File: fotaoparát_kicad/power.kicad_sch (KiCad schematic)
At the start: 41 parts

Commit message: Pridani krystalu
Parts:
- renumbered BAT+1 to BAT_IN1, BAT-1 to BAT_OUT1
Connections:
- net VDD_MIPI_DPHY is gone; now on net VDDO_3: C34.1, C39.1
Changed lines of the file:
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@@
+	(wire
+		(pts
+			(xy 36.83 163.83) (xy 35.56 163.83)
+		)
+		(stroke
+			(width 0)
+			(type default)
+		)
+	)
 	(wire
 		(pts
@@
 	(wire
 		(pts
+			(xy 22.86 163.83) (xy 22.86 165.1)
+		)
+		(stroke
+			(width 0)
+			(type default)
+		)
+	)
+	(wire
+		(pts
 			(xy 213.36 55.88) (xy 241.3 55.88)
 		)
@@
 	(wire
 		(pts
+			(xy 35.56 163.83) (xy 35.56 165.1)
+		)
+		(stroke
+			(width 0)
+			(type default)
+		)
+	)
+	(wire
+		(pts
 			(xy 241.3 44.45) (xy 241.3 45.72)
 		)
@@
 		(pts
 			(xy 78.74 55.88) (xy 78.74 62.23)
+		)
+		(stroke
+			(width 0)
+			(type default)
+		)
+	)
+	(wire
+		(pts
+			(xy 50.8 165.1) (xy 48.26 165.1)
 		)
 		(stroke
@@
 	(hierarchical_label "VDDO_FLASH"
 		(shape input)
-		(at 22.86 165.1 0)
+		(at 22.86 163.83 0)
 		(effects
 			(font
@@
 	(hierarchical_label "VDDO_PSRAM"
 		(shape input)
-		(at 35.56 165.1 0)
-		(effects
-			(font
-				(size 1.27 1.27)
-			)
-			(justify left)
-		)
-	)
-	(hierarchical_label "VDD_MIPI_DPHY"
-		(shape input)
-		(at 146.05 144.78 0)
+		(at 36.83 163.83 0)
 		(effects
 			(font
@@
 	(hierarchical_label "VDDO_3"
 		(shape input)
-		(at 48.26 165.1 0)
+		(at 50.8 165.1 0)
 		(effects
 			(font
@@
 		(shape input)
 		(at 48.26 124.46 0)
+		(effects
+			(font
+				(size 1.27 1.27)
+			)
+			(justify left)
+		)
+	)
+	(hierarchical_label "VDDO_3"
+		(shape input)
+		(at 146.05 144.78 0)
 		(effects
 			(font
@@
 		(on_board yes)
 		(dnp no)
-		(property "Reference" "BAT-1"
+		(property "Reference" "BAT_OUT1"
 			(at 89.154 64.77 0)
 			(effects
@@
 			(project "fotaoparát"
 				(path "/0ab33720-0b6a-449c-80c0-2b7abe4d9450/04ebdae2-67d7-4749-bd3e-f9c05089f6fb"
-					(reference "BAT-1")
+					(reference "BAT_OUT1")
 					(unit 1)
 				)
@@
 		(on_board yes)
 		(dnp no)
-		(property "Reference" "BAT+1"
+		(property "Reference" "BAT_IN1"
 			(at 28.194 22.86 0)
 			(effects
@@
 			(project "fotaoparát"
 				(path "/0ab33720-0b6a-449c-80c0-2b7abe4d9450/04ebdae2-67d7-4749-bd3e-f9c05089f6fb"
-					(reference "BAT+1")
+					(reference "BAT_IN1")
 					(unit 1)
 				)

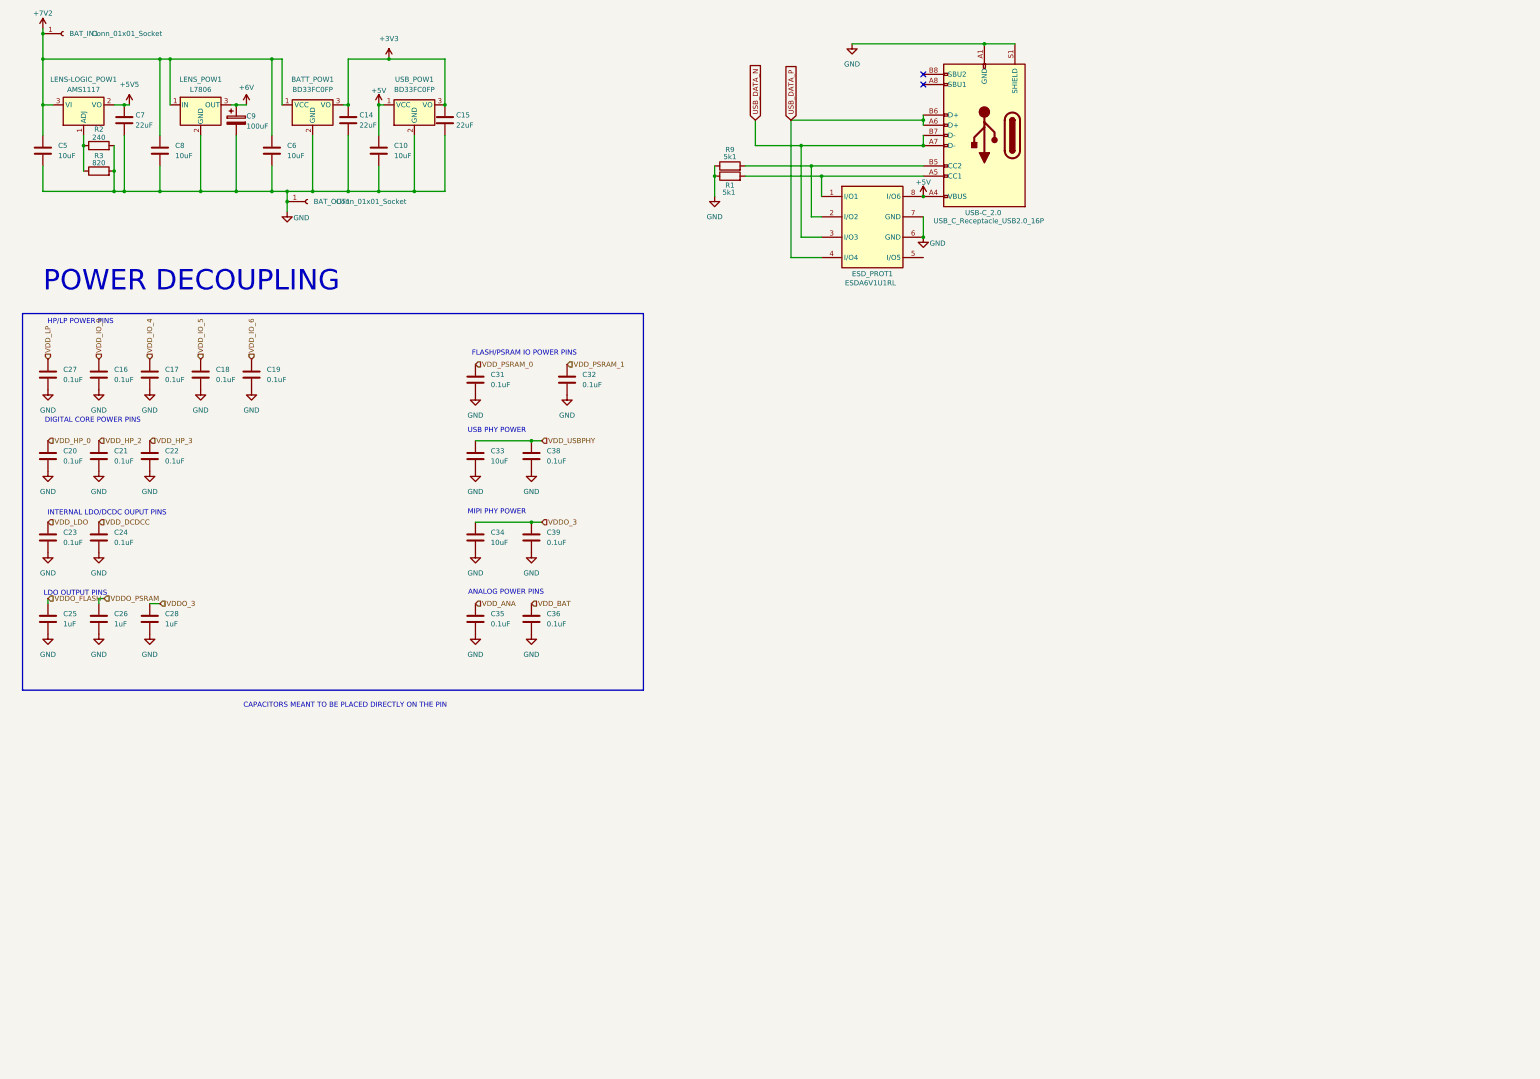
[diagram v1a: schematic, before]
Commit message: Předělání powerrials,  přidání malého pcb na spousť foťáku
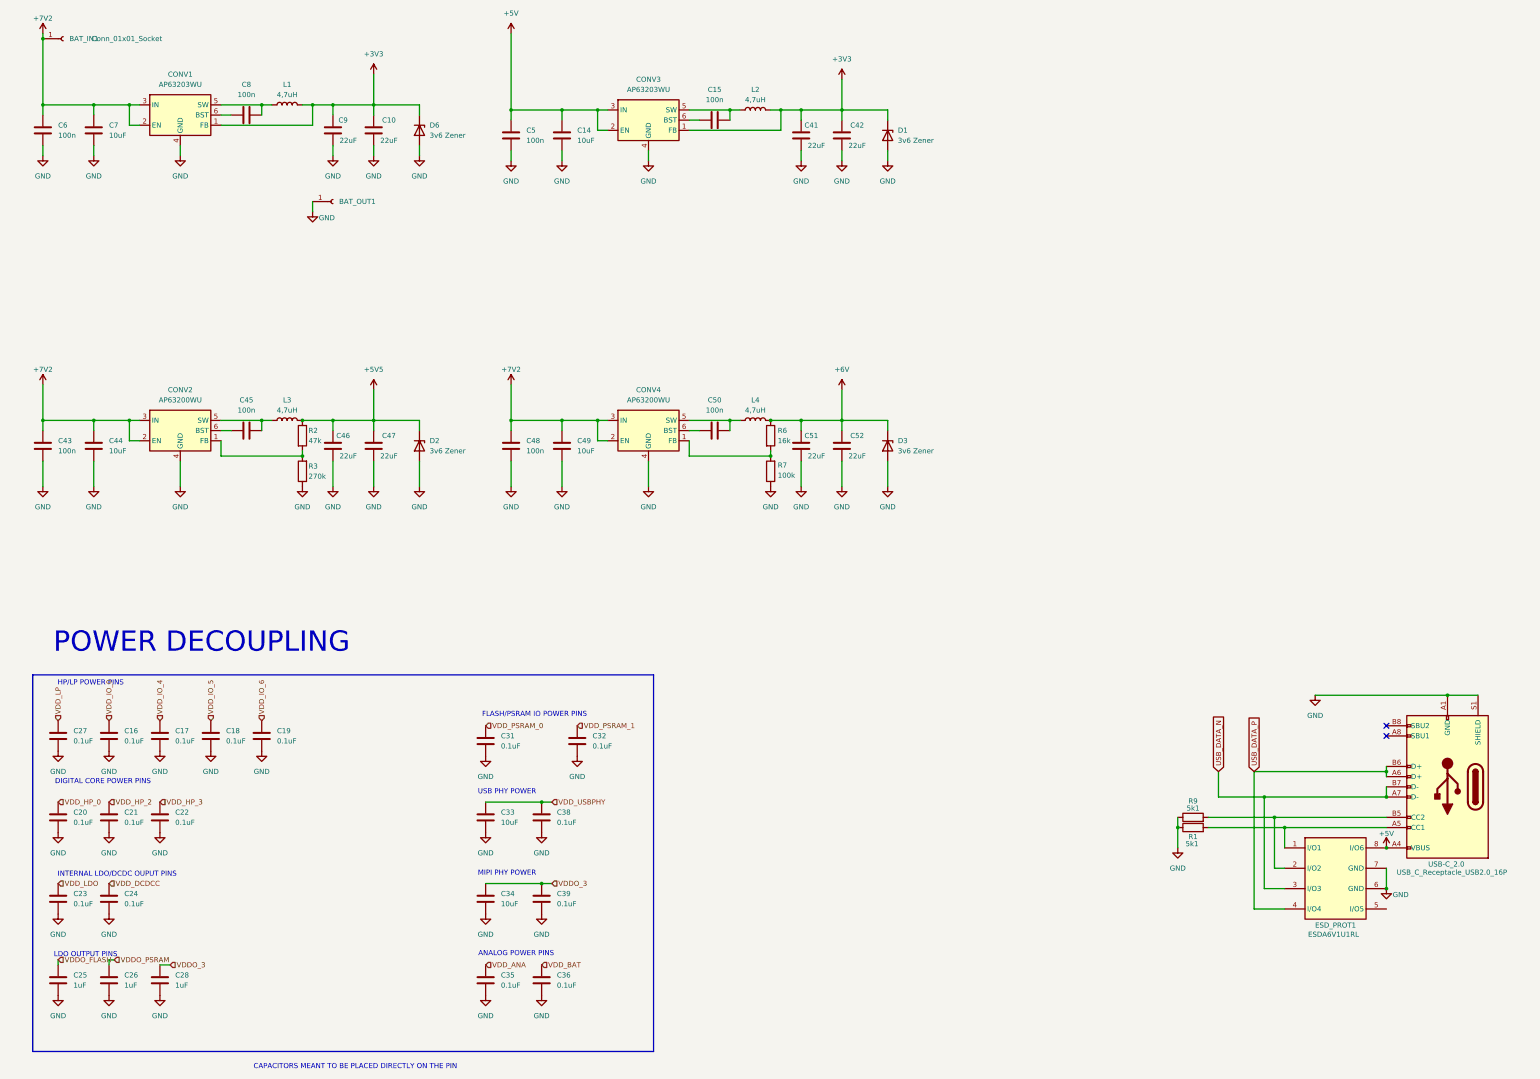
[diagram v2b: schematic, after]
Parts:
- removed BATT_POW1, USB_POW1: BD33FC0FP, Package_TO_SOT_SMD:TO-252-2, symbol Regulator_Linear:BD33FC0FP
- removed C9: 100uF, Capacitor_SMD:CP_Elec_6.3x5.4, symbol Device:C_Polarized
- removed LENS-LOGIC_POW1: AMS1117, Package_TO_SOT_SMD:SOT-223-3_TabPin2, symbol Regulator_Linear:AMS1117
- removed LENS_POW1: L7806, Package_TO_SOT_THT:TO-220-3_Horizontal_TabDown, symbol Regulator_Linear:L7806
- added C41, C42, C46, C47, C51, C52, C9: 22uF, Capacitor_SMD:C_0603_1608Metric, symbol Device:C
- added C43, C45, C48, C50: 100n, Capacitor_SMD:C_0603_1608Metric, symbol Device:C
- added C44, C49: 10uF, Capacitor_SMD:C_0603_1608Metric, symbol Device:C
- added CONV1, CONV3: AP63203WU, Package_TO_SOT_SMD:TSOT-23-6, symbol Regulator_Switching:AP63203WU
- added CONV2, CONV4: AP63200WU, Package_TO_SOT_SMD:TSOT-23-6, symbol Regulator_Switching:AP63200WU
- added D1, D2, D3, D6: 3v6 Zener, Diode_SMD:D_SOD-123, symbol Device:D_Zener
- added L1, L2, L3, L4: 4,7uH, Inductor_SMD:L_0603_1608Metric, symbol Device:L
- added R6: 16k, Resistor_SMD:R_0603_1608Metric, symbol Device:R
- added R7: 100k, Resistor_SMD:R_0603_1608Metric, symbol Device:R
- C10: value 10uF -> 22uF; footprint Capacitor_SMD:C_0201_0603Metric -> Capacitor_SMD:C_0603_1608Metric; LCSC (none) -> C59461; LCSC Part (none) -> C59461; Type (none) -> Basic
- C14, C7: value 22uF -> 10uF; footprint Capacitor_SMD:C_0201_0603Metric -> Capacitor_SMD:C_0603_1608Metric; LCSC (none) -> C19702; LCSC Part (none) -> C19702; Type (none) -> Basic
- C15: value 22uF -> 100n; footprint Capacitor_SMD:C_0201_0603Metric -> Capacitor_SMD:C_0603_1608Metric; LCSC (none) -> C14663; LCSC Part (none) -> C14663; Type (none) -> Basic
- C5, C6, C8: value 10uF -> 100n; footprint Capacitor_SMD:C_0201_0603Metric -> Capacitor_SMD:C_0603_1608Metric; LCSC (none) -> C14663; LCSC Part (none) -> C14663; Type (none) -> Basic
- R2: value 240 -> 47k
- R3: value 820 -> 270k
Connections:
- net +3V3: now also C10.2, C41.2, C42.2, C9.2, CONV1.1 (FB), CONV3.1 (FB), D1.1 (K), D6.1 (K), L1.2, L2.2; no longer C14.1, C15.1
- net +5V: now also C14.2, C5.2, CONV3.2 (EN), CONV3.3 (IN); no longer C10.1
- net +5V5: now also R2.1, C46.2, C47.2, D2.1 (K), L3.2; no longer C7.1
- net +6V: now also C51.2, C52.2, D3.1 (K), L4.2, R6.1
- net +7V2: now also C6.2, C7.2, C43.2, C44.2, C48.2, C49.2, CONV1.2 (EN), CONV1.3 (IN), CONV2.2 (EN), CONV2.3 (IN), CONV4.2 (EN), CONV4.3 (IN); no longer C5.1, C6.1, C8.1
- net GND: now also C10.1, C14.1, C5.1, C6.1, C7.1, R3.1, C41.1, C42.1, C43.1, C44.1, C46.1, C47.1, C48.1, C49.1, C51.1, C52.1, C9.1, CONV1.4 (GND), CONV2.4 (GND), CONV3.4 (GND), CONV4.4 (GND), D1.2 (A), D2.2 (A), D3.2 (A), D6.2 (A), R7.1; no longer C10.2, C14.2, C15.2, C5.2, C6.2, C7.2, C8.2, R2.2, R3.2
- new net: C8.1, CONV1.6 (BST)
- new net: C8.2, CONV1.5 (SW), L1.1
- new net: CONV2.1 (FB), R2.2, R3.2
- new net: C50.2, CONV4.5 (SW), L4.1
- new net: C45.1, CONV2.6 (BST)
- new net: C45.2, CONV2.5 (SW), L3.1
- new net: CONV4.1 (FB), R6.2, R7.2
- new net: C50.1, CONV4.6 (BST)
- new net: C15.1, CONV3.6 (BST)
- new net: C15.2, CONV3.5 (SW), L2.1
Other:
- moved on the sheet: BAT_IN1, BAT_OUT1, C16, C17, C18, C19, C20, C21, C22, C23, C24, C25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

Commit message: XDD NEVIM ZABIJU SE
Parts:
- removed C14: 10uF, Capacitor_SMD:C_0603_1608Metric, symbol Device:C
- removed C15, C5: 100n, Capacitor_SMD:C_0603_1608Metric, symbol Device:C
- removed C41, C42: 22uF, Capacitor_SMD:C_0603_1608Metric, symbol Device:C
- removed CONV3: AP63203WU, Package_TO_SOT_SMD:TSOT-23-6, symbol Regulator_Switching:AP63203WU
- removed D1: 3v6 Zener, Diode_SMD:D_SOD-123, symbol Device:D_Zener
- removed L2: 4,7uH, Inductor_SMD:L_0603_1608Metric, symbol Device:L
- added D1, D4: D_Schottky, Diode_SMD:D_0805_2012Metric, symbol Device:D_Schottky
- added J2: Conn_01x12_Pin, Connector_FFC-FPC:Hirose_FH12-11S-0.5SH_1x11-1MP_P0.50mm_Horizontal, symbol Connector:Conn_01x12_Pin
- added J3: Conn_01x12_Pin, symbol Connector:Conn_01x12_Pin
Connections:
- net +5V: now also D4.2 (A)
- net +7V2: now also D1.2 (A); no longer C6.2, C7.2, CONV1.2 (EN), CONV1.3 (IN)
- new net: C6.2, C7.2, CONV1.2 (EN), CONV1.3 (IN), D1.1 (K), D4.1 (K)
- new net: J2.1 (Pin_1), J3.1 (Pin_1)
- new net: J2.10 (Pin_10), J3.10 (Pin_10)
- new net: J2.11 (Pin_11), J3.11 (Pin_11)
- new net: J2.12 (Pin_12), J3.12 (Pin_12)
- new net: J2.2 (Pin_2), J3.2 (Pin_2)
- new net: J2.3 (Pin_3), J3.3 (Pin_3)
- new net: J2.4 (Pin_4), J3.4 (Pin_4)
- new net: J2.5 (Pin_5), J3.5 (Pin_5)
- new net: J2.6 (Pin_6), J3.6 (Pin_6)
- new net: J2.7 (Pin_7), J3.7 (Pin_7)
- new net: J2.8 (Pin_8), J3.8 (Pin_8)
- new net: J2.9 (Pin_9), J3.9 (Pin_9)
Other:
- moved on the sheet: BAT_IN1

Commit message: Pridani asi poloviny lscs cisel
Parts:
- removed J2: Conn_01x12_Pin, Connector_FFC-FPC:Hirose_FH12-11S-0.5SH_1x11-1MP_P0.50mm_Horizontal, symbol Connector:Conn_01x12_Pin
- removed J3: Conn_01x12_Pin, symbol Connector:Conn_01x12_Pin
- BAT_IN1, BAT_OUT1: now left out of the parts list
- C10, C46, C47, C51, C52, C9: LSCS Number (none) -> C2762594
- C16, C17, C18, C19, C20, C21, C22, C23, C24, C27, C31, C32, C35, C36, C38, C39: value 0.1uF -> 100nF; LSCS Number (none) -> C668346
- C25, C26, C28: LSCS Number (none) -> C307385
- C33, C34, C44, C49, C7: LSCS Number (none) -> C962136
- C43, C45, C48, C50, C6, C8: value 100n -> 100nF; LSCS Number (none) -> C66501
- CONV1: LSCS Number (none) -> C780769
- CONV2, CONV4: LSCS Number (none) -> C2071868
- D1, D4: LSCS Number (none) -> C143773
- D2, D3, D6: LSCS Number (none) -> C173412
- ESD_PROT1: LSCS Number (none) -> C118278

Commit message: PRidani (skoro) vsech lscs cisel, krystal je spatne ale pcb mam doma udelane jeste jinak, takze pridam a preroutuju pozdeji.
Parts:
- D2: value 3v6 Zener -> 5V7 Zener; LSCS Number C173412 -> C2993567
- D3: value 3v6 Zener -> 6V2 Zener; LSCS Number C173412 -> C397931
- L1: value 4,7uH -> 3,9uH; LSCS Number (none) -> C251964
- L3, L4: value 4,7uH -> 10uH; LSCS Number (none) -> C713281
- R1, R9: LSCS Number (none) -> C105580
- R2: LSCS Number (none) -> C105579
- R3: LSCS Number (none) -> C22965
- R6: LSCS Number (none) -> C137788
- R7: LSCS Number (none) -> C14675
- USB-C_2.0: LSCS Number (none) -> C53055681
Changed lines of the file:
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@@
 			)
 		)
+		(property "LSCS Number" "C22965"
+			(at 86.36 132.08 0)
+			(effects
+				(font
+					(size 1.27 1.27)
+				)
+				(hide yes)
+			)
+		)
 		(pin "2"
 		)
@@
 			)
 		)
-		(property "Value" "3v6 Zener"
+		(property "Value" "5V7 Zener"
 			(at 118.11 126.9999 90)
 			(effects
@@
 			)
 		)
-		(property "LSCS Number" "C173412"
+		(property "LSCS Number" "C2993567"
 			(at 115.57 125.73 90)
 			(effects
@@
 			)
 		)
-		(property "Value" "4,7uH"
+		(property "Value" "10uH"
 			(at 199.39 116.84 90)
 			(effects
@@
 			)
 		)
+		(property "LSCS Number" "C713281"
+			(at 199.39 119.38 90)
+			(effects
+				(font
+					(size 1.27 1.27)
+				)
+				(hide yes)
+			)
+		)
 		(pin "1"
 		)
@@
 			)
 		)
-		(property "Value" "3v6 Zener"
+		(property "Value" "6V2 Zener"
 			(at 234.95 126.9999 90)
 			(effects
@@
 			)
 		)
-		(property "LSCS Number" "C173412"
+		(property "LSCS Number" "C397931"
 			(at 232.41 125.73 90)
 			(effects
@@
 			)
 		)
+		(property "LSCS Number" "C105579"
+			(at 86.36 123.19 0)
+			(effects
+				(font
+					(size 1.27 1.27)
+				)
+				(hide yes)
+			)
+		)
 		(pin "2"
 		)
@@
 			)
 		)
+		(property "LSCS Number" "C14675"
+			(at 203.2 132.08 0)
+			(effects
+				(font
+					(size 1.27 1.27)
+				)
+				(hide yes)
+			)
+		)
 		(pin "2"
 		)
@@
 			)
 		)
+		(property "LSCS Number" "C53055681"
+			(at 372.11 210.82 0)
+			(effects
+				(font
+					(size 1.27 1.27)
+				)
+				(hide yes)
+			)
+		)
 		(pin "A9"
 		)
@@
 			)
 		)
-		(property "Value" "4,7uH"
+		(property "Value" "10uH"
 			(at 82.55 116.84 90)
 			(effects
@@
 			)
 		)
+		(property "LSCS Number" "C713281"
+			(at 82.55 119.38 90)
+			(effects
+				(font
+					(size 1.27 1.27)
+				)
+				(hide yes)
+			)
+		)
 		(pin "1"
 		)
@@
 			)
 		)
+		(property "LSCS Number" "C105580"
+			(at 308.61 218.44 90)
+			(effects
+				(font
+					(size 1.27 1.27)
+				)
+				(hide yes)
+			)
+		)
 		(pin "1"
 		)
@@
 			)
 		)
+		(property "LSCS Number" "C137788"
+			(at 203.2 123.19 0)
+			(effects
+				(font
+					(size 1.27 1.27)
+				)
+				(hide yes)
+			)
+		)
 		(pin "2"
 		)
@@
 			)
 		)
-		(property "Value" "4,7uH"
+		(property "Value" "3,9uH"
 			(at 82.55 38.1 90)
 			(effects
@@
 			)
 		)
+		(property "LSCS Number" "C251964"
+			(at 82.55 40.64 90)
+			(effects
+				(font
+					(size 1.27 1.27)
+				)
+				(hide yes)
+			)
+		)
 		(pin "1"
 		)
@@
 			(effects
 				(font
+					(size 1.27 1.27)
+				)
+				(hide yes)
+			)
+		)
+		(property "LSCS Number" "C105580"
+			(at 308.61 220.98 90)
+			(effects
+				(font
